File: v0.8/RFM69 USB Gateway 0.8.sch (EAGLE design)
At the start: 25 parts, among them CN1 MINIB, IC3 MCP1703CB, U2 ATMEGA328P-MU, X1 16 MHz

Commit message: Routed all traces
Rearranged components on the board
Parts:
- R3, R5: value 27 -> 27Ω
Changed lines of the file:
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@@
 <grid distance="0.1" unitdist="inch" unit="inch" style="lines" multiple="1" display="no" altdistance="0.01" altunitdist="inch" altunit="inch"/>
 <layers>
-<layer number="1" name="Top" color="4" fill="1" visible="yes" active="no"/>
-<layer number="2" name="Route2" color="1" fill="3" visible="yes" active="no"/>
-<layer number="3" name="Route3" color="4" fill="3" visible="yes" active="no"/>
-<layer number="4" name="Route4" color="1" fill="4" visible="yes" active="no"/>
-<layer number="5" name="Route5" color="4" fill="4" visible="yes" active="no"/>
-<layer number="6" name="Route6" color="1" fill="8" visible="yes" active="no"/>
-<layer number="7" name="Route7" color="4" fill="8" visible="yes" active="no"/>
-<layer number="8" name="Route8" color="1" fill="2" visible="yes" active="no"/>
-<layer number="9" name="Route9" color="4" fill="2" visible="yes" active="no"/>
-<layer number="10" name="Route10" color="1" fill="7" visible="yes" active="no"/>
-<layer number="11" name="Route11" color="4" fill="7" visible="yes" active="no"/>
-<layer number="12" name="Route12" color="1" fill="5" visible="yes" active="no"/>
-<layer number="13" name="Route13" color="4" fill="5" visible="yes" active="no"/>
-<layer number="14" name="Route14" color="1" fill="6" visible="yes" active="no"/>
-<layer number="15" name="Route15" color="4" fill="6" visible="yes" active="no"/>
-<layer number="16" name="Bottom" color="1" fill="1" visible="yes" active="no"/>
-<layer number="17" name="Pads" color="2" fill="1" visible="yes" active="no"/>
-<layer number="18" name="Vias" color="2" fill="1" visible="yes" active="no"/>
-<layer number="19" name="Unrouted" color="6" fill="1" visible="yes" active="no"/>
-<layer number="20" name="Dimension" color="15" fill="1" visible="yes" active="no"/>
-<layer number="21" name="tPlace" color="16" fill="1" visible="yes" active="no"/>
-<layer number="22" name="bPlace" color="14" fill="1" visible="yes" active="no"/>
-<layer number="23" name="tOrigins" color="15" fill="1" visible="yes" active="no"/>
-<layer number="24" name="bOrigins" color="15" fill="1" visible="yes" active="no"/>
-<layer number="25" name="tNames" color="7" fill="1" visible="yes" active="no"/>
-<layer number="26" name="bNames" color="7" fill="1" visible="yes" active="no"/>
-<layer number="27" name="tValues" color="7" fill="1" visible="yes" active="no"/>
-<layer number="28" name="bValues" color="7" fill="1" visible="yes" active="no"/>
+<layer number="1" name="Top" color="4" fill="1" visible="no" active="no"/>
+<layer number="2" name="Route2" color="1" fill="3" visible="no" active="no"/>
+<layer number="3" name="Route3" color="4" fill="3" visible="no" active="no"/>
+<layer number="4" name="Route4" color="1" fill="4" visible="no" active="no"/>
+<layer number="5" name="Route5" color="4" fill="4" visible="no" active="no"/>
+<layer number="6" name="Route6" color="1" fill="8" visible="no" active="no"/>
+<layer number="7" name="Route7" color="4" fill="8" visible="no" active="no"/>
+<layer number="8" name="Route8" color="1" fill="2" visible="no" active="no"/>
+<layer number="9" name="Route9" color="4" fill="2" visible="no" active="no"/>
+<layer number="10" name="Route10" color="1" fill="7" visible="no" active="no"/>
+<layer number="11" name="Route11" color="4" fill="7" visible="no" active="no"/>
+<layer number="12" name="Route12" color="1" fill="5" visible="no" active="no"/>
+<layer number="13" name="Route13" color="4" fill="5" visible="no" active="no"/>
+<layer number="14" name="Route14" color="1" fill="6" visible="no" active="no"/>
+<layer number="15" name="Route15" color="4" fill="6" visible="no" active="no"/>
+<layer number="16" name="Bottom" color="1" fill="1" visible="no" active="no"/>
+<layer number="17" name="Pads" color="2" fill="1" visible="no" active="no"/>
+<layer number="18" name="Vias" color="2" fill="1" visible="no" active="no"/>
+<layer number="19" name="Unrouted" color="6" fill="1" visible="no" active="no"/>
+<layer number="20" name="Dimension" color="15" fill="1" visible="no" active="no"/>
+<layer number="21" name="tPlace" color="16" fill="1" visible="no" active="no"/>
+<layer number="22" name="bPlace" color="14" fill="1" visible="no" active="no"/>
+<layer number="23" name="tOrigins" color="15" fill="1" visible="no" active="no"/>
+<layer number="24" name="bOrigins" color="15" fill="1" visible="no" active="no"/>
+<layer number="25" name="tNames" color="7" fill="1" visible="no" active="no"/>
+<layer number="26" name="bNames" color="7" fill="1" visible="no" active="no"/>
+<layer number="27" name="tValues" color="7" fill="1" visible="no" active="no"/>
+<layer number="28" name="bValues" color="7" fill="1" visible="no" active="no"/>
 <layer number="29" name="tStop" color="7" fill="3" visible="no" active="no"/>
 <layer number="30" name="bStop" color="7" fill="6" visible="no" active="no"/>
@@
 <layer number="35" name="tGlue" color="7" fill="4" visible="no" active="no"/>
 <layer number="36" name="bGlue" color="7" fill="5" visible="no" active="no"/>
-<layer number="37" name="tTest" color="7" fill="1" visible="yes" active="no"/>
-<layer number="38" name="bTest" color="7" fill="1" visible="yes" active="no"/>
+<layer number="37" name="tTest" color="7" fill="1" visible="no" active="no"/>
+<layer number="38" name="bTest" color="7" fill="1" visible="no" active="no"/>
 <layer number="39" name="tKeepout" color="4" fill="11" visible="no" active="no"/>
 <layer number="40" name="bKeepout" color="1" fill="11" visible="no" active="no"/>
@@
 <layer number="44" name="Drills" color="7" fill="1" visible="no" active="no"/>
 <layer number="45" name="Holes" color="7" fill="1" visible="no" active="no"/>
-<layer number="46" name="Milling" color="3" fill="1" visible="yes" active="no"/>
-<layer number="47" name="Measures" color="7" fill="1" visible="yes" active="no"/>
-<layer number="48" name="Document" color="7" fill="1" visible="yes" active="no"/>
-<layer number="49" name="Reference" color="7" fill="1" visible="yes" active="no"/>
-<layer number="50" name="dxf" color="7" fill="1" visible="yes" active="no"/>
-<layer number="51" name="tDocu" color="6" fill="1" visible="yes" active="no"/>
-<layer number="52" name="bDocu" color="13" fill="1" visible="yes" active="no"/>
-<layer number="53" name="tGND_GNDA" color="7" fill="9" visible="yes" active="no"/>
-<layer number="54" name="bGND_GNDA" color="1" fill="9" visible="yes" active="no"/>
-<layer number="56" name="wert" color="7" fill="1" visible="yes" active="no"/>
-<layer number="57" name="tCAD" color="7" fill="1" visible="yes" active="no"/>
-<layer number="59" name="tCarbon" color="7" fill="1" visible="yes" active="no"/>
-<layer number="60" name="bCarbon" color="7" fill="1" visible="yes" active="no"/>
+<layer number="46" name="Milling" color="3" fill="1" visible="no" active="no"/>
+<layer number="47" name="Measures" color="7" fill="1" visible="no" active="no"/>
+<layer number="48" name="Document" color="7" fill="1" visible="no" active="no"/>
+<layer number="49" name="Reference" color="7" fill="1" visible="no" active="no"/>
+<layer number="50" name="dxf" color="7" fill="1" visible="no" active="no"/>
+<layer number="51" name="tDocu" color="6" fill="1" visible="no" active="no"/>
+<layer number="52" name="bDocu" color="13" fill="1" visible="no" active="no"/>
+<layer number="53" name="tGND_GNDA" color="7" fill="9" visible="no" active="no"/>
+<layer number="54" name="bGND_GNDA" color="1" fill="9" visible="no" active="no"/>
+<layer number="56" name="wert" color="7" fill="1" visible="no" active="no"/>
+<layer number="57" name="tCAD" color="7" fill="1" visible="no" active="no"/>
+<layer number="59" name="tCarbon" color="7" fill="1" visible="no" active="no"/>
+<layer number="60" name="bCarbon" color="7" fill="1" visible="no" active="no"/>
 <layer number="90" name="Modules" color="5" fill="1" visible="yes" active="yes"/>
 <layer number="91" name="Nets" color="2" fill="1" visible="yes" active="yes"/>
@@
 <part name="SUPPLY16" library="supply2" deviceset="GND" device=""/>
 <part name="D" library="LowPowerLab" deviceset="RESISTOR" device="0805" value="SHOTTKY"/>
-<part name="R3" library="SparkFun" deviceset="RESISTOR" device="0805-RES" value="27"/>
-<part name="R5" library="SparkFun" deviceset="RESISTOR" device="0805-RES" value="27"/>
+<part name="R3" library="SparkFun" deviceset="RESISTOR" device="0805-RES" value="27Ω"/>
+<part name="R5" library="SparkFun" deviceset="RESISTOR" device="0805-RES" value="27Ω"/>
 <part name="JP1" library="pinhead" deviceset="PINHD-2X3" device=""/>
 <part name="SUPPLY1" library="SparkFun" deviceset="VCC" device="" value="3.3V"/>

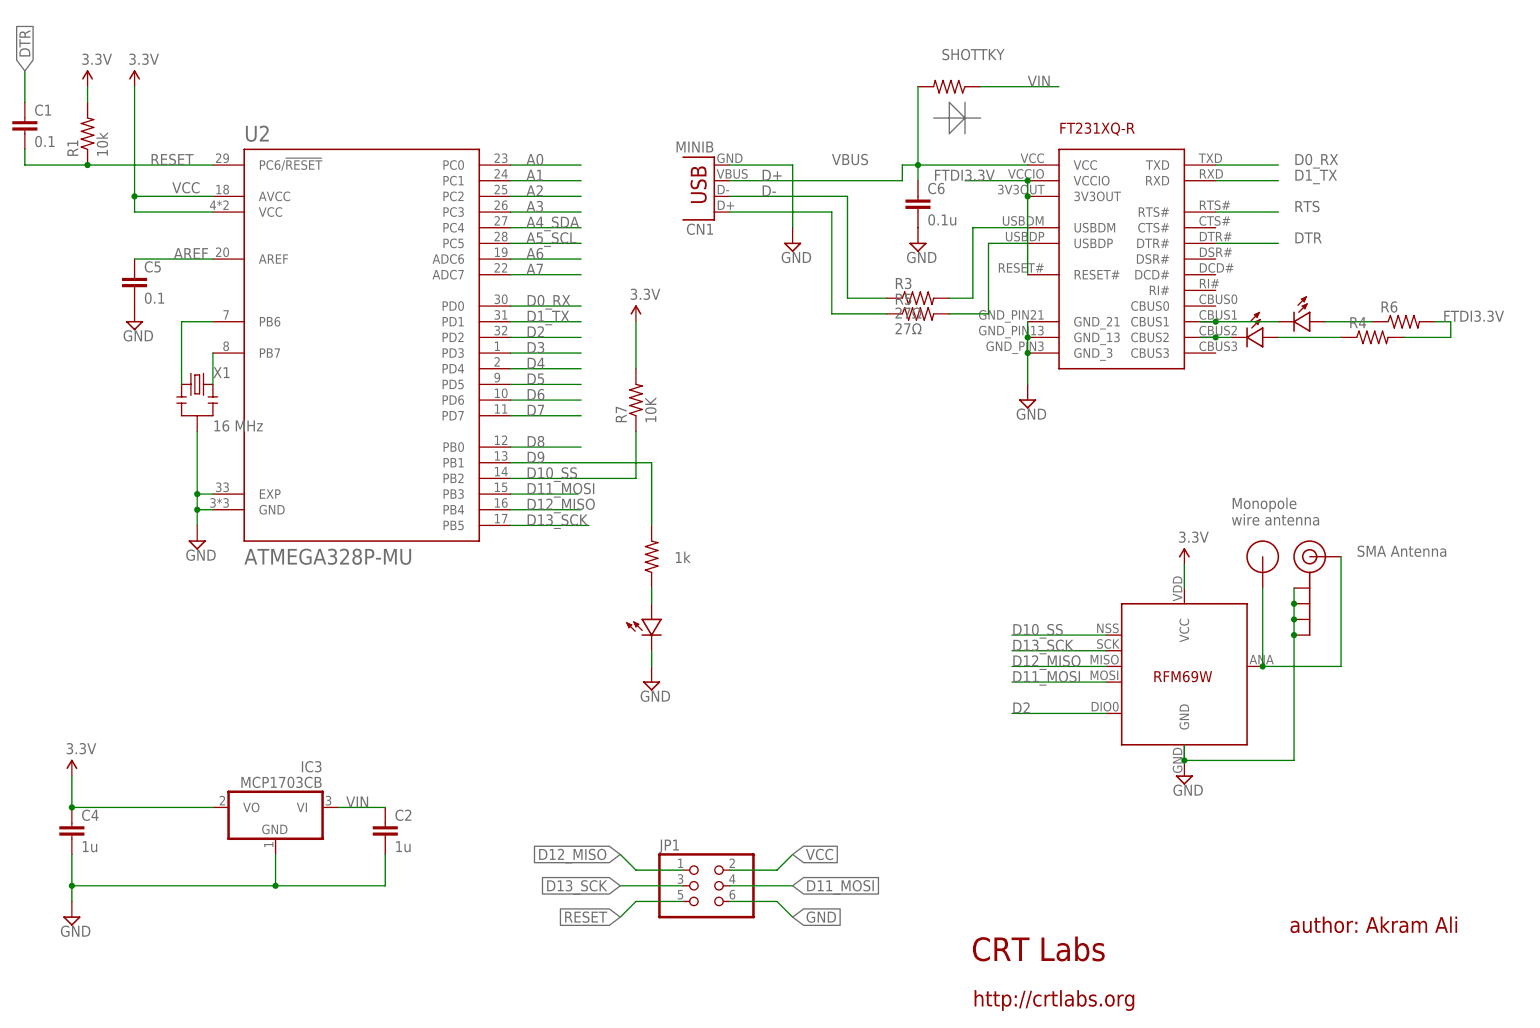
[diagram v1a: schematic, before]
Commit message: Unsmashed and updated all component values
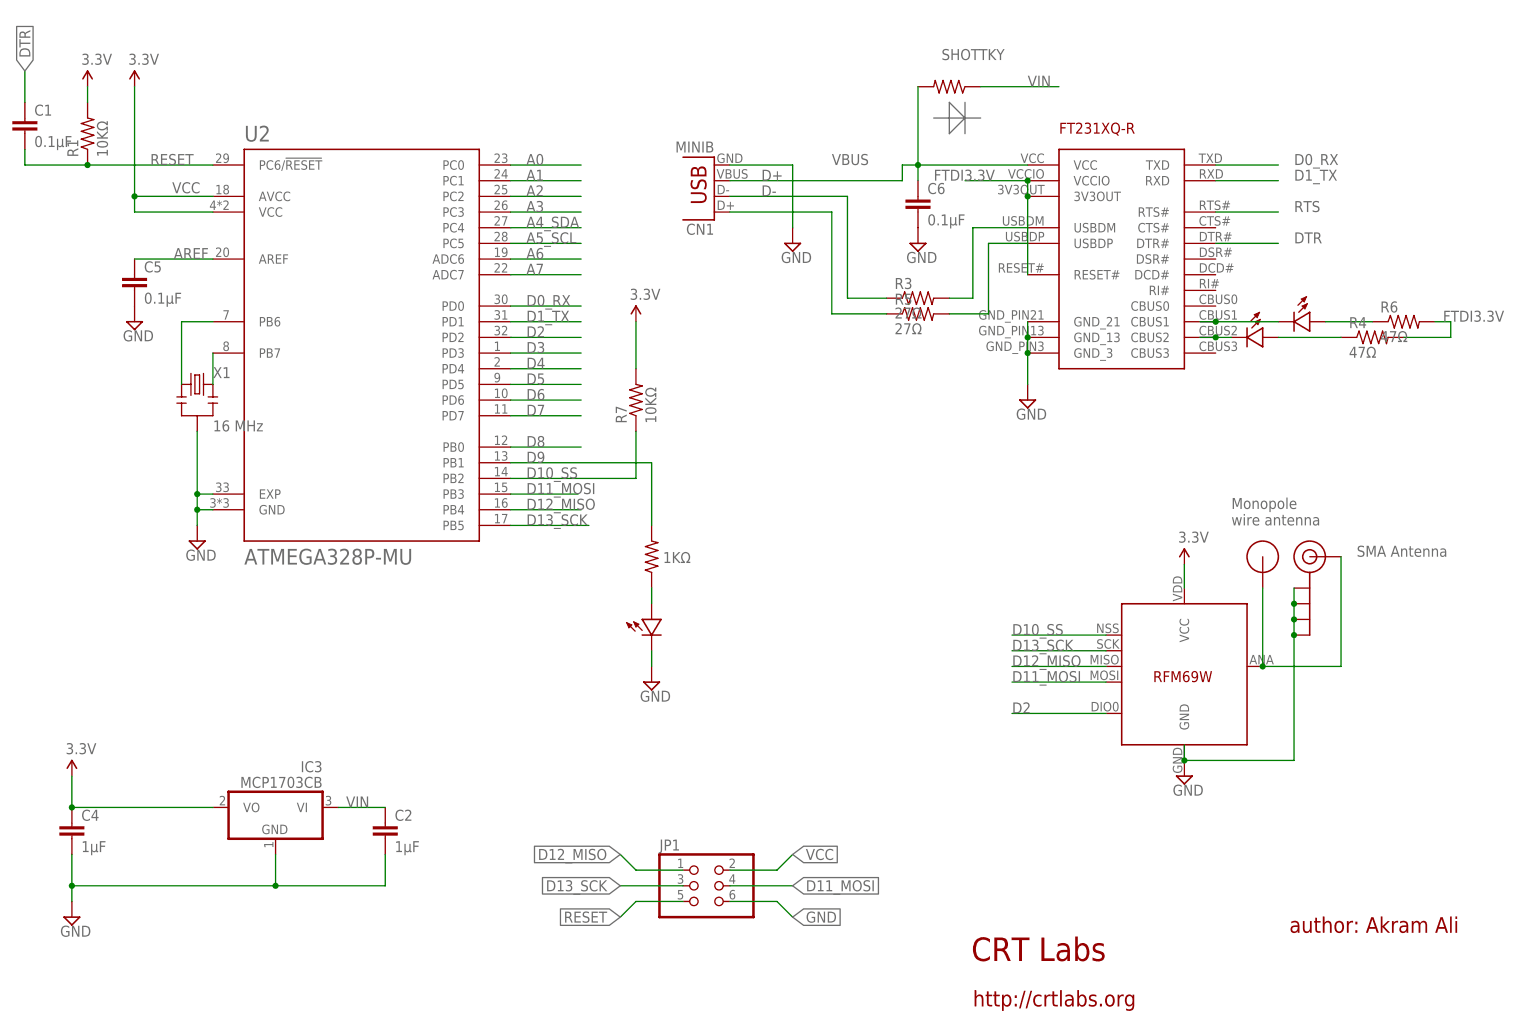
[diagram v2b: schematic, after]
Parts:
- C1, C5: value 0.1 -> 0.1μF
- C2, C4: value 1u -> 1μF
- C6: value 0.1u -> 0.1μF
- R1: value 10k -> 10KΩ
- R2: value 1k -> 1KΩ
- R4, R6: value (none) -> 47Ω
- R7: value 10K -> 10KΩ
- RX: value LED0805 -> Green
- TX: value LED0805 -> Red
- renumbered U$4 to RX, U$7 to TX
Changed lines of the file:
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@@
 <part name="P+1" library="SparkFun" deviceset="VCC" device="" value="3.3V"/>
 <part name="IC3" library="linear" deviceset="MCP1703" device="CB"/>
-<part name="C5" library="SparkFun" deviceset="CAP" device="0805" value="0.1"/>
-<part name="R1" library="LowPowerLab" deviceset="RESISTOR" device="0805" value="10k"/>
-<part name="C4" library="LowPowerLab" deviceset="CAP" device="0805" value="1u"/>
-<part name="C2" library="SparkFun" deviceset="CAP" device="0805" value="1u"/>
+<part name="C5" library="SparkFun" deviceset="CAP" device="0805" value="0.1μF"/>
+<part name="R1" library="LowPowerLab" deviceset="RESISTOR" device="0805" value="10KΩ"/>
+<part name="C4" library="LowPowerLab" deviceset="CAP" device="0805" value="1μF"/>
+<part name="C2" library="SparkFun" deviceset="CAP" device="0805" value="1μF"/>
 <part name="U$2" library="LowPowerLab" deviceset="LED" device="0805" value="LED0805"/>
 <part name="SUPPLY6" library="supply2" deviceset="GND" device=""/>
-<part name="R2" library="SparkFun" deviceset="RESISTOR" device="0805-RES" value="1k"/>
+<part name="R2" library="SparkFun" deviceset="RESISTOR" device="0805-RES" value="1KΩ"/>
 <part name="U$1" library="LowPowerLab" deviceset="RFM12B_ANTENNA" device=""/>
 <part name="U$5" library="LowPowerLab" deviceset="RFM69" device=""/>
 <part name="CN1" library="SparkFun-Connectors" deviceset="USB" device="-A-H" value="MINIB"/>
-<part name="R4" library="SparkFun" deviceset="RESISTOR" device="0805-RES"/>
-<part name="R6" library="SparkFun" deviceset="RESISTOR" device="0805-RES"/>
-<part name="U$4" library="LowPowerLab" deviceset="LED" device="0805" value="LED0805"/>
-<part name="U$7" library="LowPowerLab" deviceset="LED" device="0805" value="LED0805"/>
-<part name="C6" library="SparkFun" deviceset="CAP" device="0805" value="0.1u"/>
+<part name="R4" library="SparkFun" deviceset="RESISTOR" device="0805-RES" value="47Ω"/>
+<part name="R6" library="SparkFun" deviceset="RESISTOR" device="0805-RES" value="47Ω"/>
+<part name="RX" library="LowPowerLab" deviceset="LED" device="0805" value="Green"/>
+<part name="TX" library="LowPowerLab" deviceset="LED" device="0805" value="Red"/>
+<part name="C6" library="SparkFun" deviceset="CAP" device="0805" value="0.1μF"/>
 <part name="SUPPLY9" library="supply2" deviceset="GND" device=""/>
 <part name="SUPPLY12" library="supply2" deviceset="GND" device=""/>
@@
 <part name="JP1" library="pinhead" deviceset="PINHD-2X3" device=""/>
 <part name="SUPPLY1" library="SparkFun" deviceset="VCC" device="" value="3.3V"/>
-<part name="R7" library="SparkFun" deviceset="RESISTOR" device="0805-RES" value="10K"/>
+<part name="R7" library="SparkFun" deviceset="RESISTOR" device="0805-RES" value="10KΩ"/>
 <part name="P+2" library="SparkFun" deviceset="VCC" device="" value="3.3V"/>
-<part name="C1" library="SparkFun" deviceset="CAP" device="0805" value="0.1"/>
+<part name="C1" library="SparkFun" deviceset="CAP" device="0805" value="0.1μF"/>
 <part name="J$1" library="SparkFun-Connectors" deviceset="SMA_EDGE" device=""/>
 <part name="U2" library="ATMEGA328P-MU" deviceset="ATMEGA328P-MU" device=""/>
@@
 <instance part="R4" gate="G$1" x="231.14" y="116.84"/>
 <instance part="R6" gate="G$1" x="236.22" y="119.38"/>
-<instance part="U$4" gate="G$1" x="218.44" y="119.38"/>
-<instance part="U$7" gate="G$1" x="210.82" y="116.84"/>
+<instance part="RX" gate="G$1" x="218.44" y="119.38"/>
+<instance part="TX" gate="G$1" x="210.82" y="116.84"/>
 <instance part="C6" gate="G$1" x="157.48" y="137.16"/>
 <instance part="SUPPLY9" gate="GND" x="137.16" y="132.08"/>
@@
 <segment>
 <wire x1="215.9" y1="119.38" x2="205.74" y2="119.38" width="0.1524" layer="91"/>
-<pinref part="U$4" gate="G$1" pin="MINUS"/>
+<pinref part="RX" gate="G$1" pin="MINUS"/>
 <pinref part="FT231XQ-R" gate="G$1" pin="CBUS1"/>
 <wire x1="205.74" y1="119.38" x2="203.2" y2="119.38" width="0.1524" layer="91"/>
@@
 <segment>
 <wire x1="205.74" y1="116.84" x2="203.2" y2="116.84" width="0.1524" layer="91"/>
-<pinref part="U$7" gate="G$1" pin="MINUS"/>
+<pinref part="TX" gate="G$1" pin="MINUS"/>
 <pinref part="FT231XQ-R" gate="G$1" pin="CBUS2"/>
 <junction x="205.74" y="116.84"/>
@@
 <wire x1="226.06" y1="116.84" x2="215.9" y2="116.84" width="0.1524" layer="91"/>
 <pinref part="R4" gate="G$1" pin="1"/>
-<pinref part="U$7" gate="G$1" pin="PLUS"/>
+<pinref part="TX" gate="G$1" pin="PLUS"/>
 </segment>
 </net>
@@
 <segment>
 <wire x1="231.14" y1="119.38" x2="223.52" y2="119.38" width="0.1524" layer="91"/>
-<pinref part="U$4" gate="G$1" pin="PLUS"/>
+<pinref part="RX" gate="G$1" pin="PLUS"/>
 <pinref part="R6" gate="G$1" pin="1"/>
 </segment>
